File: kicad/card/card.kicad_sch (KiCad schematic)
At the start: 6 parts, among them U1 RP2350_60QFN, U2 TLV70030_SOT23-5, U3 BNO086

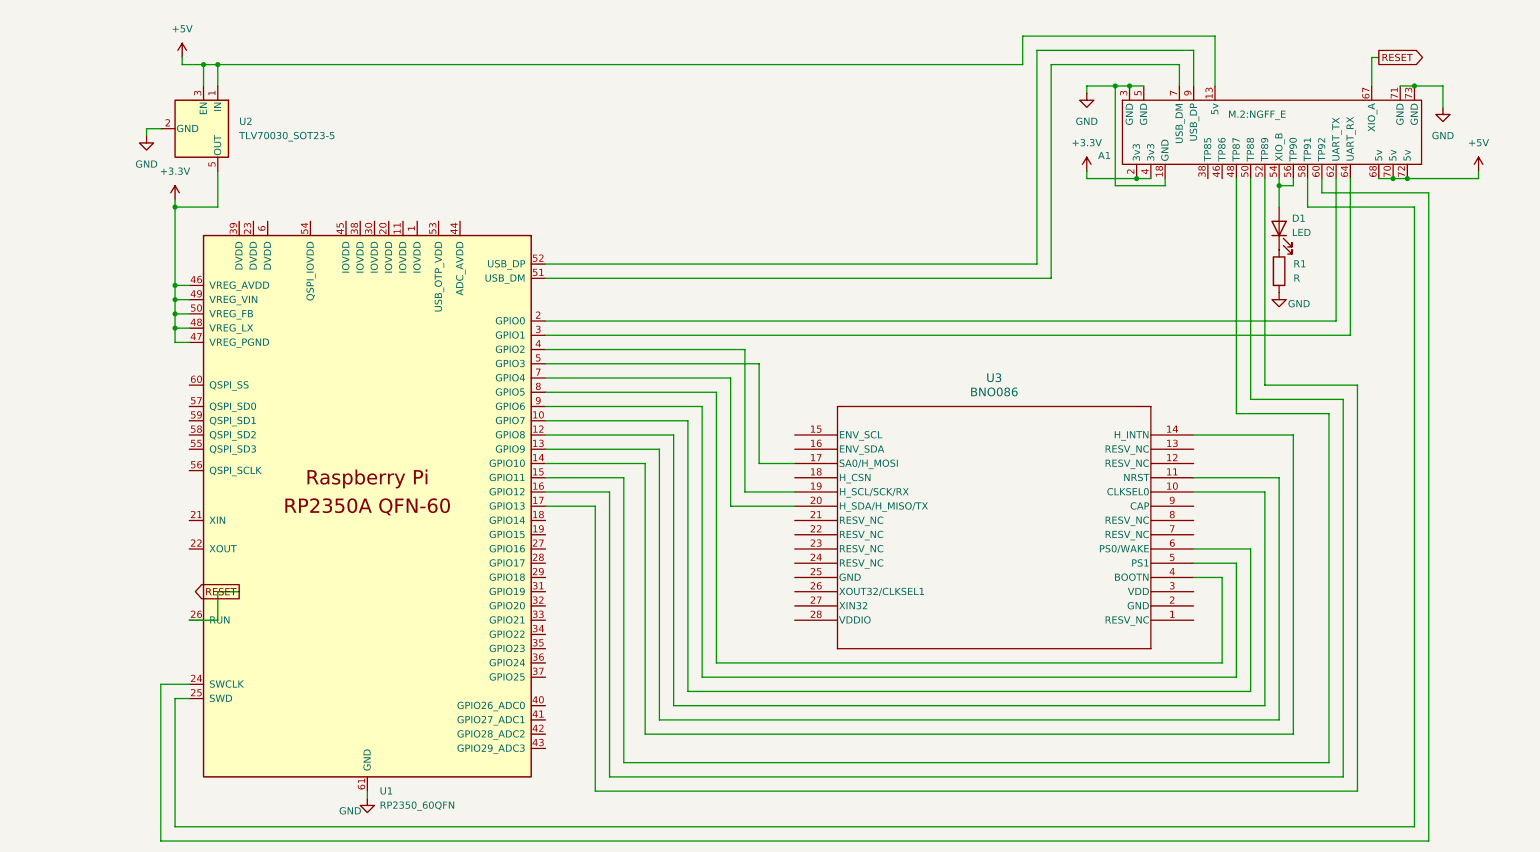
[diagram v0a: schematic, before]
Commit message: minimal "blink" bring up revised schematic and starting with new components to place
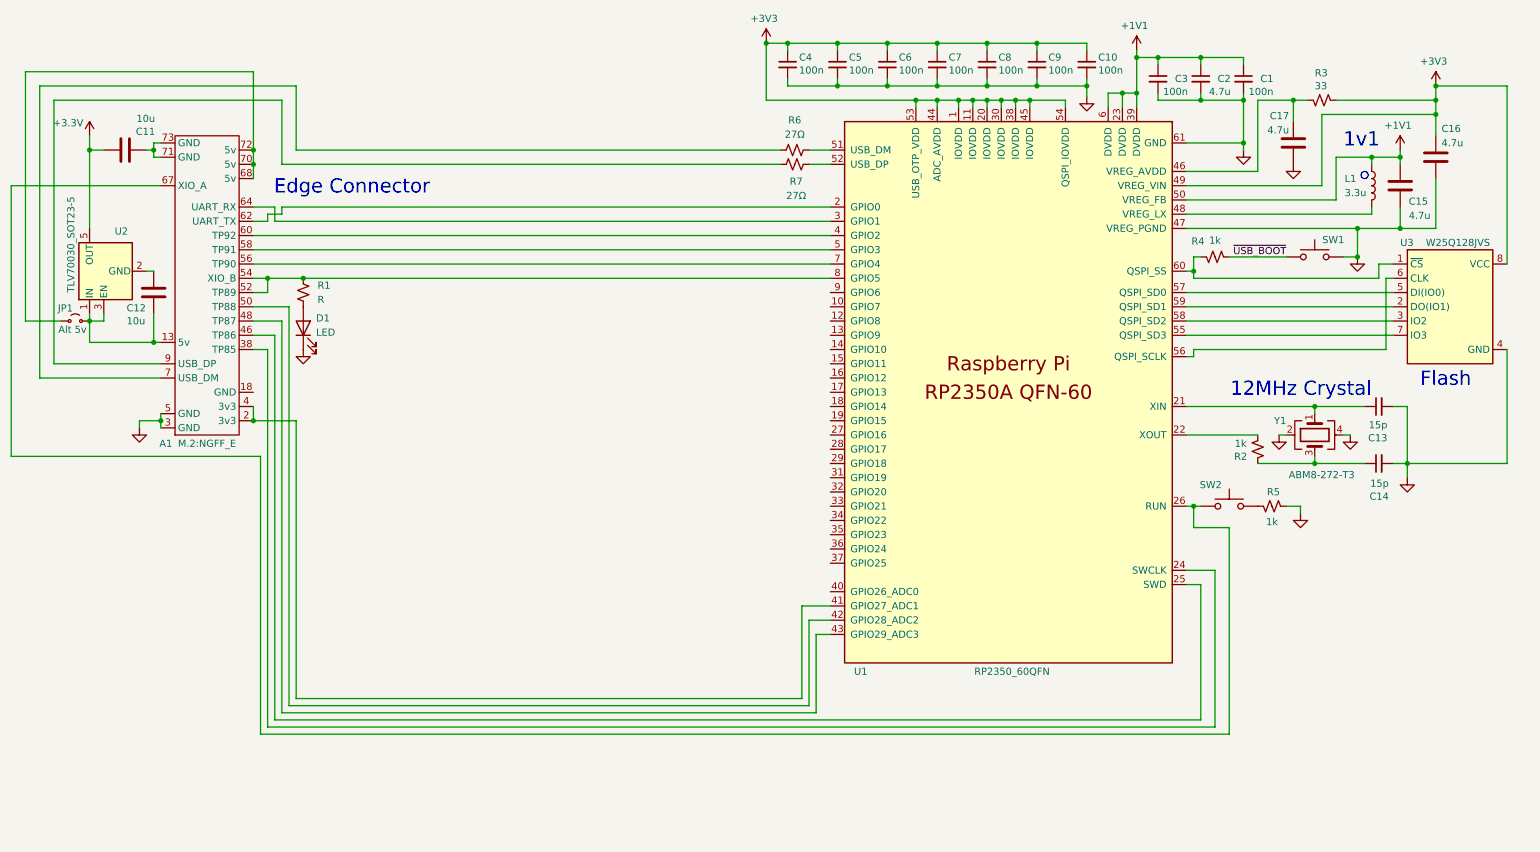
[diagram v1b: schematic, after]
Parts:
- removed U3: BNO086, QFN28_BNO086_CEV, symbol 2024-10-24_23-43-15:BNO086
- added C1, C10, C3, C4, C5, C6, C7, C8, C9: 100n, Capacitor_SMD:C_0402_1005Metric, symbol Device:C_Small
- added C11, C12: 10u, Capacitor_SMD:C_0805_2012Metric, symbol Device:C
- added C13, C14: 15p, Capacitor_SMD:C_0402_1005Metric, symbol Device:C_Small
- added C15, C16: 4.7u, RP2350_60QFN_minimal:C_0402_1005Metric_small_pads, symbol Device:C
- added C17: 4.7u, Capacitor_SMD:C_0402_1005Metric, symbol Device:C
- added C2: 4.7u, Capacitor_SMD:C_0402_1005Metric, symbol Device:C_Small
- added JP1: Alt 5v, symbol Jumper:Jumper_2_Small_Open
- added L1: 3.3u, RP2350_60QFN_minimal:L_pol_2016, symbol Device:L
- added R2, R4, R5: 1k, Resistor_SMD:R_0402_1005Metric, symbol Device:R_Small_US
- added R3: 33, Resistor_SMD:R_0402_1005Metric, symbol Device:R_Small_US
- added R6, R7: 27Ω, symbol Device:R_Small_US
- added SW1, SW2: SW_Push, Button_Switch_SMD:SW_Push_1P1T_NO_Vertical_Wuerth_434133025816, symbol Switch:SW_Push
- added U3: W25Q128JVS, Package_SO:SOIC-8_5.23x5.23mm_P1.27mm, symbol Memory_Flash:W25Q128JVS
- added Y1: ABM8-272-T3, Crystal:Crystal_SMD_3225-4Pin_3.2x2.5mm, symbol Device:Crystal_GND24
- R1: symbol Device:R -> Device:R_Small_US
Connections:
- net +3.3V: now also C11.1; no longer A1.2 (3v3), A1.4 (3v3), U1.46 (VREG_AVDD), U1.47 (VREG_PGND), U1.48 (VREG_LX), U1.49 (VREG_VIN), U1.50 (VREG_FB)
- net GND: now also D1.1 (K), U1.47 (VREG_PGND), C1.2, C10.2, C13.2, C14.2, C15.2, C16.2, C17.2, C2.2, C3.2, C4.2, C5.2, C6.2, C7.2, C8.2, C9.2, R5.2, SW1.1, U3.4 (GND), Y1.2, Y1.4; no longer A1.18 (GND), A1.71 (GND), A1.73 (GND), R1.2, U2.2 (GND)
- net at U1.5 (GPIO3): now also A1.58 (TP91)
- net at U1.4 (GPIO2): now also A1.60 (TP92)
- net at U1.7 (GPIO4): now also A1.56 (TP90)
- net at U1.8 (GPIO5): now also A1.52 (TP89), A1.54 (XIO_B), R1.1
- net +3V3: now reaches U1.1 (IOVDD)
- net +3V3: now also U1.11 (IOVDD), U1.20 (IOVDD), U1.30 (IOVDD), U1.38 (IOVDD), U1.44 (ADC_AVDD), U1.45 (IOVDD), U1.49 (VREG_VIN), U1.53 (USB_OTP_VDD), U1.54 (QSPI_IOVDD), C10.1, C16.1, C4.1, C5.1, C6.1, C7.1, C8.1, C9.1, R3.1, U3.8 (VCC)
- net at U1.15 (GPIO11): no longer A1.48 (TP87)
- net at U1.16 (GPIO12): no longer A1.50 (TP88)
- net at U1.17 (GPIO13): no longer A1.52 (TP89)
- net at U1.21 (XIN): now also C13.1, Y1.1
- net at U1.22 (XOUT): now also R2.2
- net +1V1: now reaches U1.23 (DVDD)
- net +1V1: now also U1.39 (DVDD), U1.50 (VREG_FB), U1.6 (DVDD), C1.1, C15.1, C2.1, C3.1, L1.1
- net at U1.24 (SWCLK): now also A1.38 (TP85); no longer A1.60 (TP92)
- net at U1.25 (SWD): now also A1.46 (TP86); no longer A1.58 (TP91)
- net at U1.41 (GPIO27_ADC1): now also A1.2 (3v3), A1.4 (3v3)
- net at U1.42 (GPIO28_ADC2): now also A1.50 (TP88)
- net at U1.43 (GPIO29_ADC3): now also A1.48 (TP87)
- net at A1.7 (USB_DM): now also R6.1; no longer U1.51 (USB_DM)
- net at U1.52 (USB_DP): now also R7.1; no longer A1.9 (USB_DP)
- net at U1.55 (QSPI_SD3): now also U3.7 (IO3)
- net at U1.56 (QSPI_SCLK): now also U3.6 (CLK)
- net at U1.57 (QSPI_SD0): now also U3.5 (DI(IO0))
- net at U1.58 (QSPI_SD2): now also U3.3 (IO2)
- net at U1.59 (QSPI_SD1): now also U3.2 (DO(IO1))
- net at U1.60 (QSPI_SS): now also R4.1, U3.1 (~{CS})
- net +5V: no longer names the net of A1.68 (5v), A1.70 (5v), A1.72 (5v)
- net +5V: now also JP1.1 (A); no longer A1.13 (5v), U2.1 (IN), U2.3 (EN)
- net RESET: no longer names the net of A1.67 (XIO_A), U1.26 (RUN)
- net RESET: now also SW2.2
- new net: C14.1, R2.1, Y1.3
- new net: A1.13 (5v), C12.2, JP1.2 (B), U2.1 (IN), U2.3 (EN)
- new net: C12.1, U2.2 (GND)
- new net: R6.2, U1.51 (USB_DM)
- new net: C17.1, R3.2, U1.46 (VREG_AVDD)
- new net: L1.2, U1.48 (VREG_LX)
- new net: D1.2 (A), R1.2
- new net: R5.1, SW2.1
- new net: A1.9 (USB_DP), R7.2
- new net: A1.71 (GND), A1.73 (GND), C11.2
- new net ~{USB_BOOT}: R4.2, SW1.2
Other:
- note added: "12MHz Crystal"
- note added: "1v1"
- note added: "Edge Connector"
- note added: "Flash"
- company: (none) -> DEFAULT
- title: (none) -> minimal blink layout
- moved on the sheet: A1, D1, U1, U2

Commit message: compentents positioned in lower half of PCB
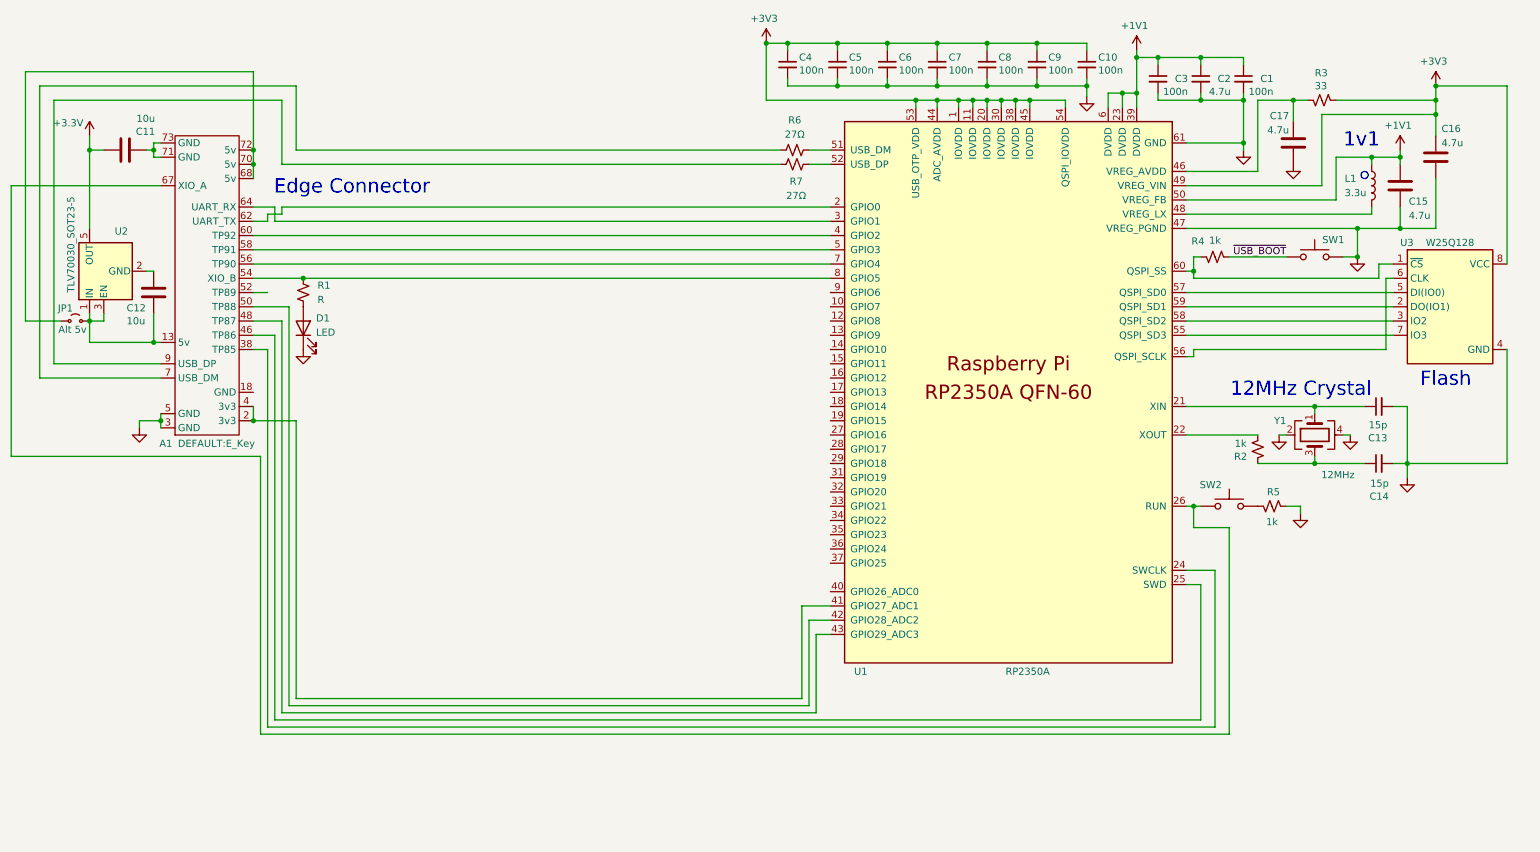
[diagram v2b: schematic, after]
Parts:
- A1: footprint M.2:NGFF_E -> DEFAULT:E_Key
- D1: footprint LED_SMD:LED_0805_2012Metric -> LED_SMD:LED_0603_1608Metric_Pad1.05x0.95mm_HandSolder
- JP1: footprint (none) -> Jumper:SolderJumper-2_P1.3mm_Open_TrianglePad1.0x1.5mm
- R1: footprint Resistor_SMD:R_0805_2012Metric -> Resistor_SMD:R_0603_1608Metric_Pad0.98x0.95mm_HandSolder
- R6, R7: footprint (none) -> Resistor_SMD:R_0402_1005Metric
- SW1: value SW_Push -> USB_BOOT
- SW2: value SW_Push -> RESET
- U1: value RP2350_60QFN -> RP2350A
- U3: value W25Q128JVS -> W25Q128
- Y1: value ABM8-272-T3 -> 12MHz
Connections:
- net at A1.54 (XIO_B), R1.1, U1.8 (GPIO5): no longer A1.52 (TP89)
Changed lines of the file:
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@@
 	)
 	(junction
-		(at 59.69 62.23)
-		(diameter 0)
-		(color 0 0 0 0)
-	)
-	(junction
 		(at 196.85 27.94)
 		(diameter 0)
@@
 	(wire
 		(pts
-			(xy 59.69 62.23) (xy 66.04 62.23)
+			(xy 57.15 62.23) (xy 66.04 62.23)
 		)
 		(stroke
@@
 	(wire
 		(pts
-			(xy 57.15 62.23) (xy 59.69 62.23)
-		)
-		(stroke
-			(width 0)
-			(type default)
-		)
-	)
-	(wire
-		(pts
 			(xy 62.23 49.53) (xy 160.02 49.53)
 		)
@@
 	(wire
 		(pts
-			(xy 59.69 64.77) (xy 59.69 62.23)
-		)
-		(stroke
-			(width 0)
-			(type default)
-		)
-	)
-	(wire
-		(pts
 			(xy 187.96 26.67) (xy 187.96 27.94)
 		)
@@
 			)
 		)
-		(property "Value" "SW_Push"
+		(property "Value" "USB_BOOT"
 			(at 246.38 53.34 0)
 			(effects
@@
 			)
 		)
-		(property "Footprint" ""
+		(property "Footprint" "Jumper:SolderJumper-2_P1.3mm_Open_TrianglePad1.0x1.5mm"
 			(at 25.4 69.85 0)
 			(effects
@@
 			)
 		)
-		(property "Footprint" ""
+		(property "Footprint" "Resistor_SMD:R_0402_1005Metric"
 			(at 153.67 39.37 0)
 			(effects
@@
 			)
 		)
-		(property "Value" "RP2350_60QFN"
+		(property "Value" "RP2350A"
 			(at 199.136 132.334 0)
 			(effects
@@
 			)
 		)
-		(property "Value" "ABM8-272-T3"
+		(property "Value" "12MHz"
 			(at 253.492 97.282 90)
 			(effects
@@
 			)
 		)
-		(property "Description" ""
+		(property "Description" "ABM8-272-T3"
 			(at 246.38 90.17 0)
 			(effects
@@
 			)
 		)
-		(property "Value" "W25Q128JVS"
+		(property "Value" "W25Q128"
 			(at 266.192 55.88 0)
 			(effects
@@
 			)
 		)
-		(property "Footprint" "Resistor_SMD:R_0805_2012Metric"
+		(property "Footprint" "Resistor_SMD:R_0603_1608Metric_Pad0.98x0.95mm_HandSolder"
 			(at 66.04 64.77 0)
 			(effects
@@
 			)
 		)
-		(property "Footprint" "LED_SMD:LED_0805_2012Metric"
+		(property "Footprint" "LED_SMD:LED_0603_1608Metric_Pad1.05x0.95mm_HandSolder"
 			(at 66.04 71.12 0)
 			(effects
@@
 			)
 		)
-		(property "Value" "SW_Push"
+		(property "Value" "RESET"
 			(at 231.14 98.7861 0)
 			(effects
@@
 			)
 		)
-		(property "Footprint" ""
+		(property "Footprint" "Resistor_SMD:R_0402_1005Metric"
 			(at 153.67 41.91 0)
 			(effects
@@
 		(on_board yes)
 		(dnp no)
+		(fields_autoplaced yes)
 		(property "Reference" "A1"
 			(at 40.386 91.694 90)
@@
 			)
 		)
-		(property "Footprint" "M.2:NGFF_E"
+		(property "Footprint" "DEFAULT:E_Key"
 			(at 43.688 91.694 90)
 			(effects

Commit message: mostly routed, USB & +5V alt?
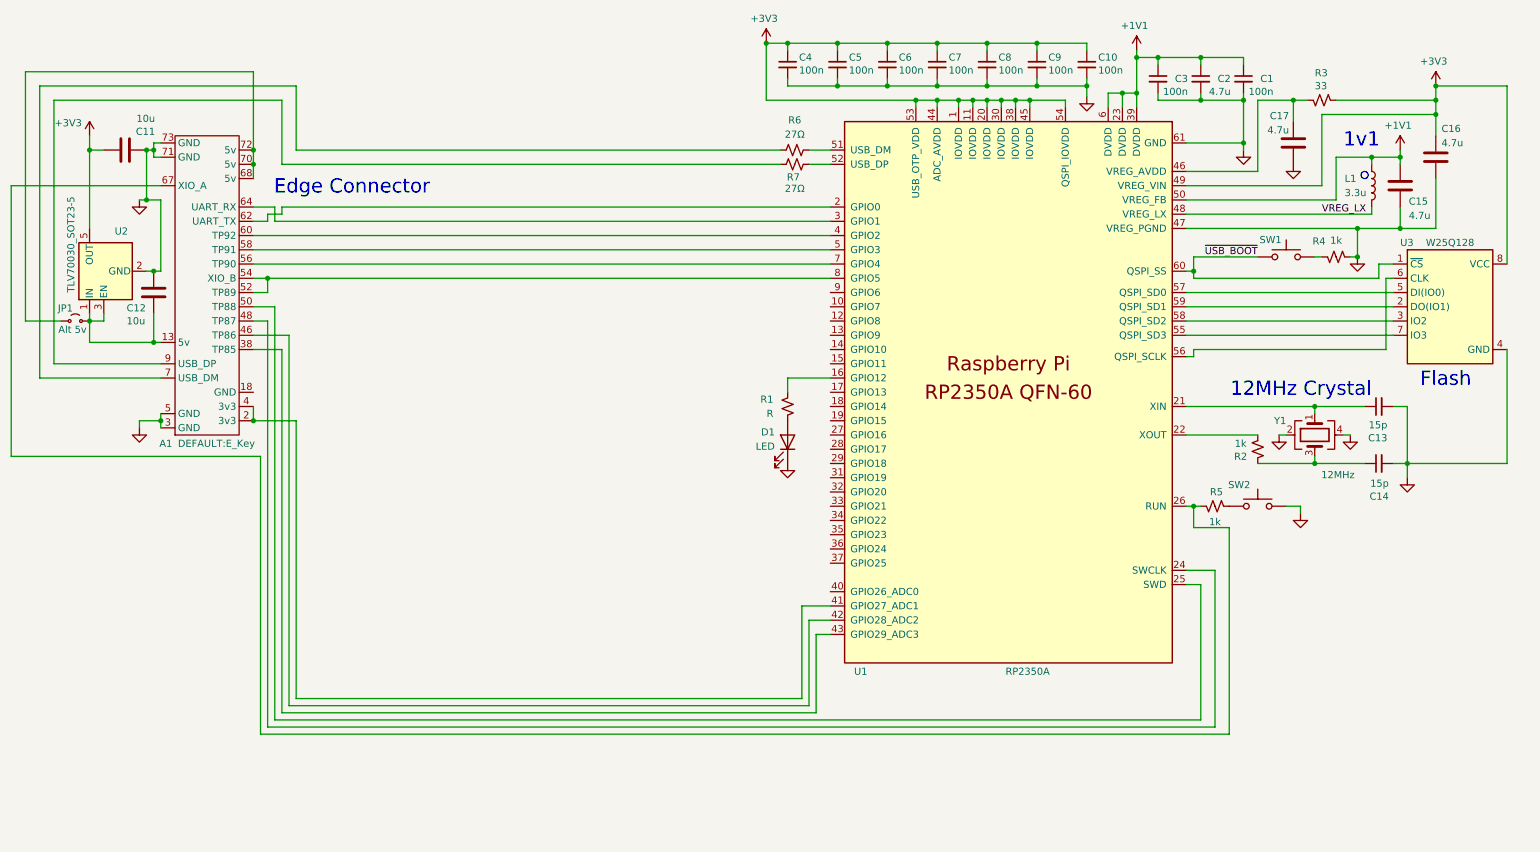
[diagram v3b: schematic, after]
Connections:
- net +3.3V is gone; now on net +3V3: C11.1, U2.5 (OUT)
- net GND: now also A1.71 (GND), A1.73 (GND), C11.2, C12.1, R4.2, SW2.1, U2.2 (GND); no longer R5.2, SW1.1
- net ~{USB_BOOT}: now also U1.60 (QSPI_SS), U3.1 (~{CS}); no longer R4.2
- net at U1.16 (GPIO12): now also R1.1
- net at U1.24 (SWCLK): now also A1.48 (TP87); no longer A1.38 (TP85)
- net at U1.25 (SWD): now also A1.50 (TP88); no longer A1.46 (TP86)
- net at A1.67 (XIO_A), U1.26 (RUN): now also R5.1; no longer SW2.2
- net at U1.42 (GPIO28_ADC2): now also A1.46 (TP86); no longer A1.50 (TP88)
- net at U1.43 (GPIO29_ADC3): now also A1.38 (TP85); no longer A1.48 (TP87)
- net VREG_LX: now reaches L1.2, U1.48 (VREG_LX)
- net at U1.52 (USB_DP): now also R7.2; no longer R7.1
- net at A1.54 (XIO_B), U1.8 (GPIO5): now also A1.52 (TP89); no longer R1.1
- net at A1.9 (USB_DP): now also R7.1; no longer R7.2
- new net: R4.1, SW1.1
- new net: R5.2, SW2.2
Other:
- moved on the sheet: D1, R1, R4, R5, R7, SW1, SW2

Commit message: routed, 5V alt and IMU stub
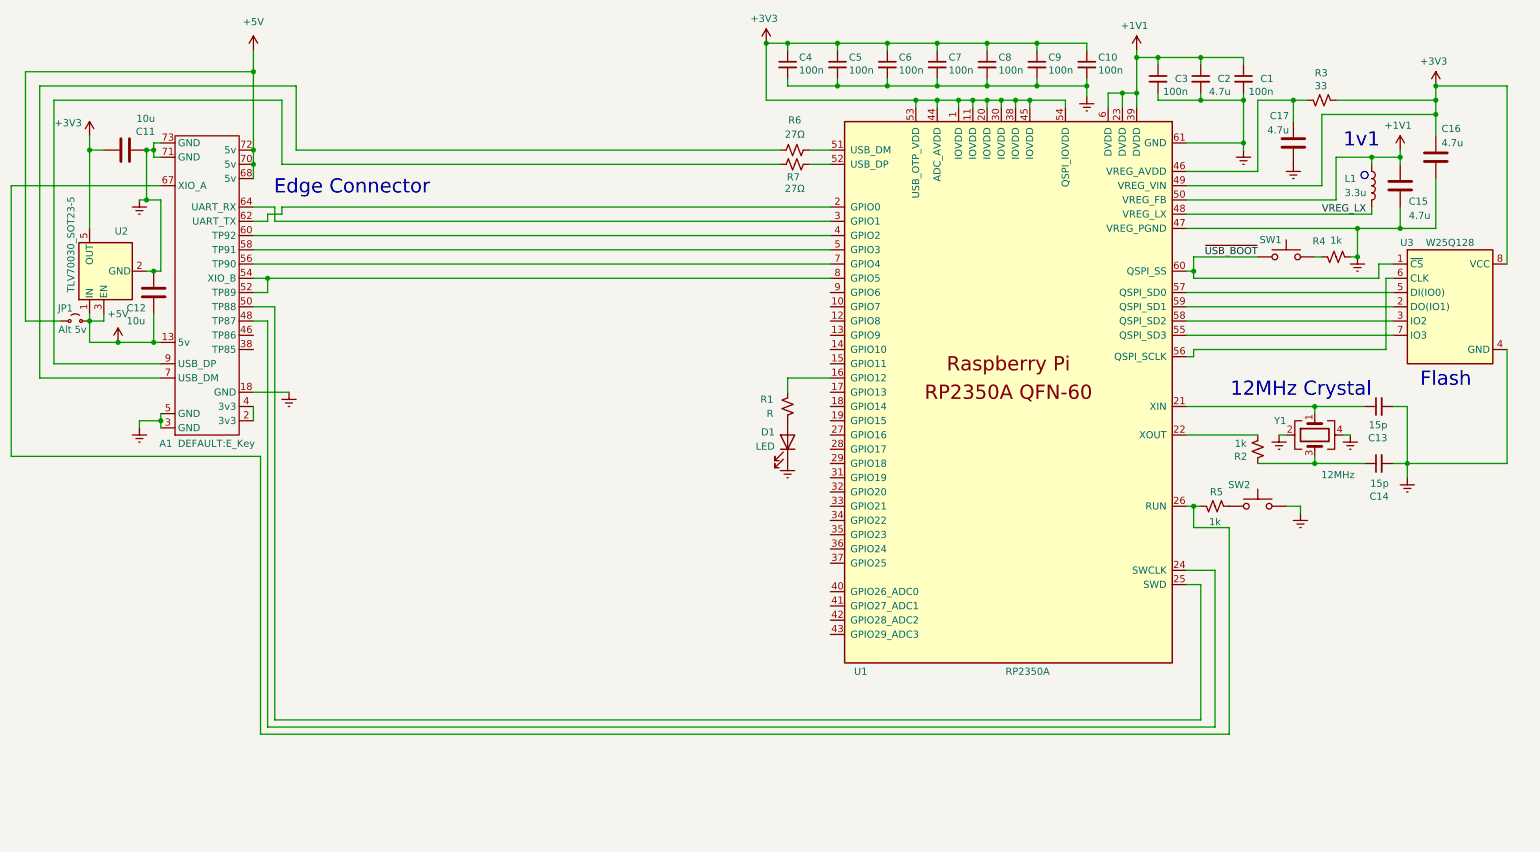
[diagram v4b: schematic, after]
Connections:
- net GND: now also A1.18 (GND)
- net +5V: now reaches A1.68 (5v), A1.70 (5v), A1.72 (5v), JP1.1 (A)
- net +5V: now also A1.13 (5v), C12.2, JP1.2 (B), U2.1 (IN), U2.3 (EN)
- net at A1.2 (3v3), A1.4 (3v3): no longer U1.41 (GPIO27_ADC1)
- net at U1.42 (GPIO28_ADC2): no longer A1.46 (TP86)
- net at U1.43 (GPIO29_ADC3): no longer A1.38 (TP85)
